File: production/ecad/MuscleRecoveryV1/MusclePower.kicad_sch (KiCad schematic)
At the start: 0 parts

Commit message: Added fuel guage schematic, may need adjustments
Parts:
- added C1: 1uF, symbol Device:C
- added CONN3G$1, CONN4G$1: Screw_Terminal_01x04, symbol Connector:Screw_Terminal_01x04
- added D1: GREEN, symbol Device:LED
- added IC1: LC709203FQH-01TWG, Package_DFN_QFN:WDFN-8-1EP_4x3mm_P0.65mm_EP2.4x1.8mm, symbol Battery_Management:LC709203FQH-01TWG
- added J1: Screw_Terminal_01x06, symbol Connector:Screw_Terminal_01x06
- added J2, J3: Screw_Terminal_01x02, symbol Connector:Screw_Terminal_01x02
- added R1, R3G$2, R3G$3: 10K, Resistor_SMD:R_0805_2012Metric, symbol Device:R
- added R3G$1, R3G$4: 10K, symbol Device:R
- added R4: 100, Resistor_SMD:R_0805_2012Metric, symbol Device:R
- added SJ1: SolderJumper_2_Open, symbol Jumper:SolderJumper_2_Open
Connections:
- new net: IC1.5 (T_{SW}), R4.1
- new net: R1.2, R4.2
- new net: IC1.6 (T_{SENSE}), R1.1
- new net: D1.1 (K), R3G$4.1
- new net: D1.2 (A), SJ1.1 (A)
- new net GND: C1.2, CONN3G$1.4 (Pin_4), CONN4G$1.4 (Pin_4), IC1.1 (TEST), IC1.2 (V_{SS}), J1.2 (Pin_2), J2.1 (Pin_1), J3.1 (Pin_1), R3G$4.2
- new net INT: IC1.4 (~{ALARMB}), J1.5 (Pin_5), R3G$3.2
- new net SCL: CONN3G$1.1 (Pin_1), CONN4G$1.1 (Pin_1), IC1.8 (SCL), J1.3 (Pin_3), R3G$1.2
- new net SDA: CONN3G$1.2 (Pin_2), CONN4G$1.2 (Pin_2), IC1.7 (SDA), J1.4 (Pin_4), R3G$2.2
- new net THERM: J1.6 (Pin_6)
- new net VCC: CONN3G$1.3 (Pin_3), CONN4G$1.3 (Pin_3), J1.1 (Pin_1), R3G$1.1, R3G$2.1, R3G$3.1, SJ1.2 (B)
- new net VDD: C1.1, J2.2 (Pin_2), J3.2 (Pin_2)

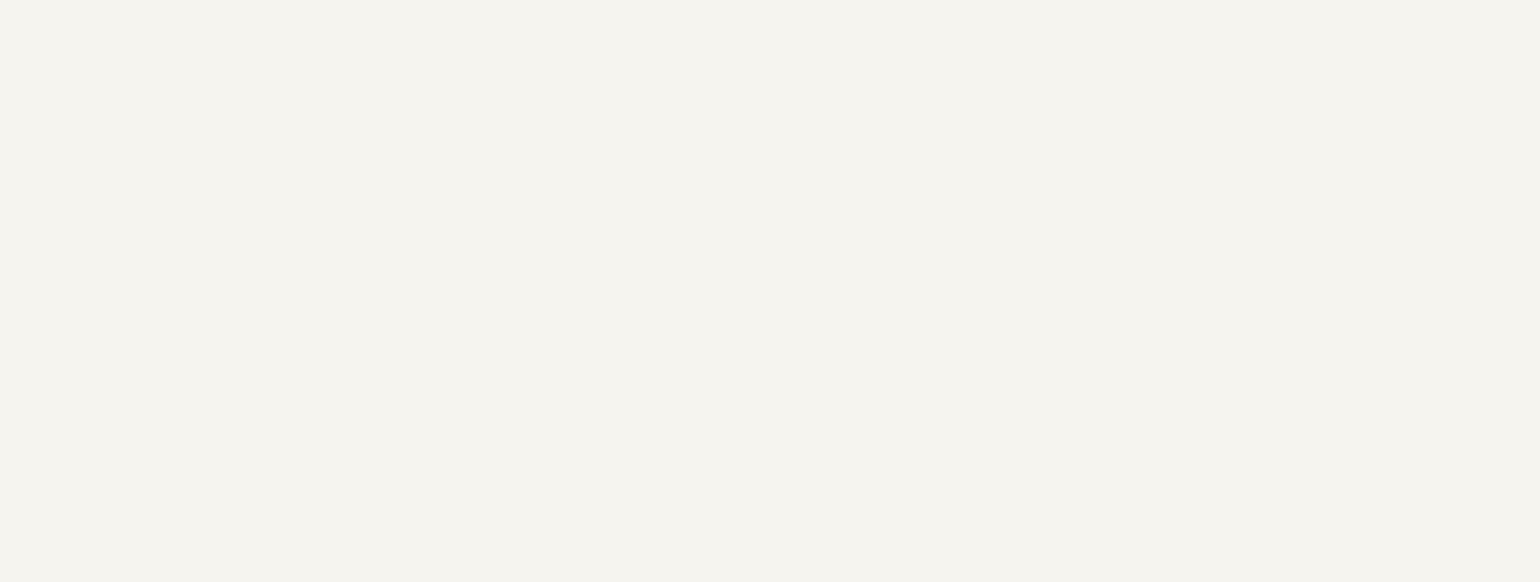
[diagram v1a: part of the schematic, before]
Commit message: Combined schematics together
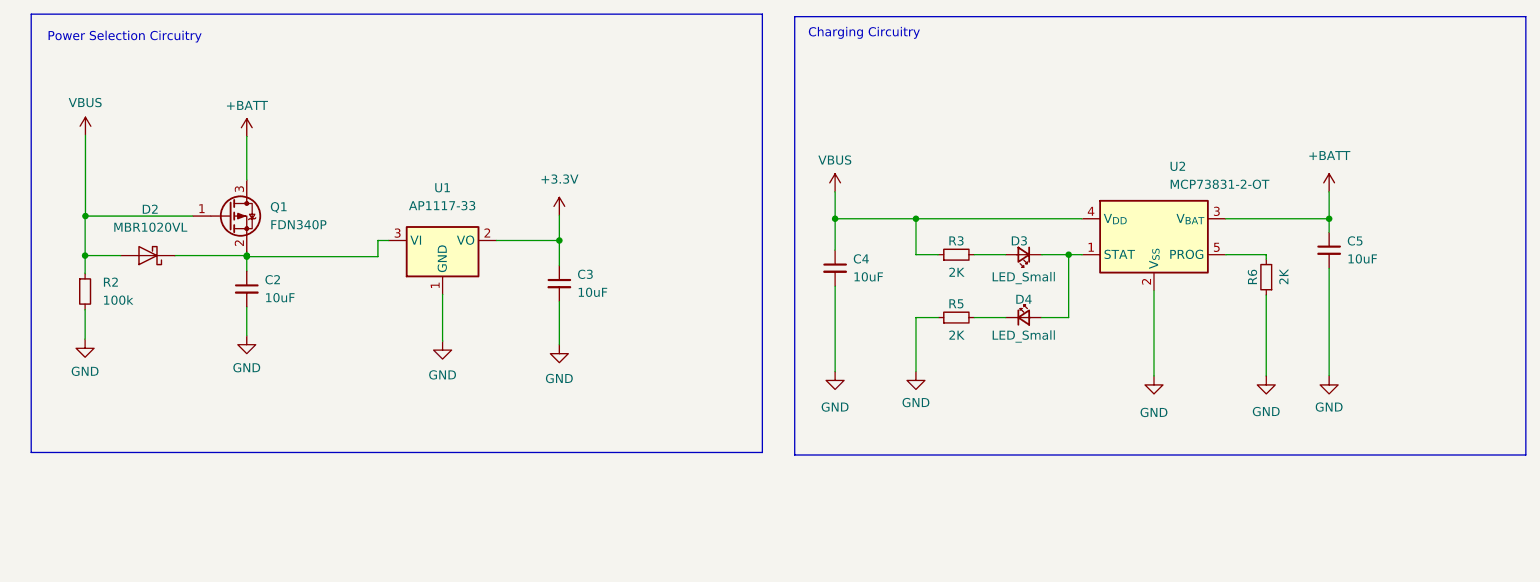
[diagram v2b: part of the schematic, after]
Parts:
- added C2, C3, C4, C5: 10uF, symbol Device:C_Small
- added D2: MBR1020VL, Diode_SMD:D_SOD-123F, symbol Diode:MBR1020VL
- added D3, D4: LED_Small, symbol Device:LED_Small
- added Q1: FDN340P, Package_TO_SOT_SMD:SOT-23, symbol Transistor_FET:FDN340P
- added R2: 100k, symbol Device:R_Small
- added R3, R5, R6: 2K, symbol Device:R_Small
- added U1: AP1117-33, Package_TO_SOT_SMD:SOT-223-3_TabPin2, symbol Regulator_Linear:AP1117-33
- added U2: MCP73831-2-OT, Package_TO_SOT_SMD:SOT-23-5, symbol Battery_Management:MCP73831-2-OT
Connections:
- net GND: now also C2.2, C3.2, C4.2, C5.2, R2.2, R5.1, R6.1, U1.1 (GND), U2.2 (V_{SS})
- new net: C2.1, D2.1 (K), Q1.2 (S), U1.3 (VI)
- new net: D4.1 (K), R5.2
- new net: D3.1 (K), D4.2 (A), U2.1 (STAT)
- new net: D3.2 (A), R3.2
- new net: R6.2, U2.5 (PROG)
- new net +3.3V: C3.1, U1.2 (VO)
- new net +BATT: C5.1, Q1.3 (D), U2.3 (V_{BAT})
- new net VBUS: C4.1, D2.2 (A), Q1.1 (G), R2.1, R3.1, U2.4 (V_{DD})
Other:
- note added: "Charging Circuitry"
- note added: "Power Selection Circuitry"

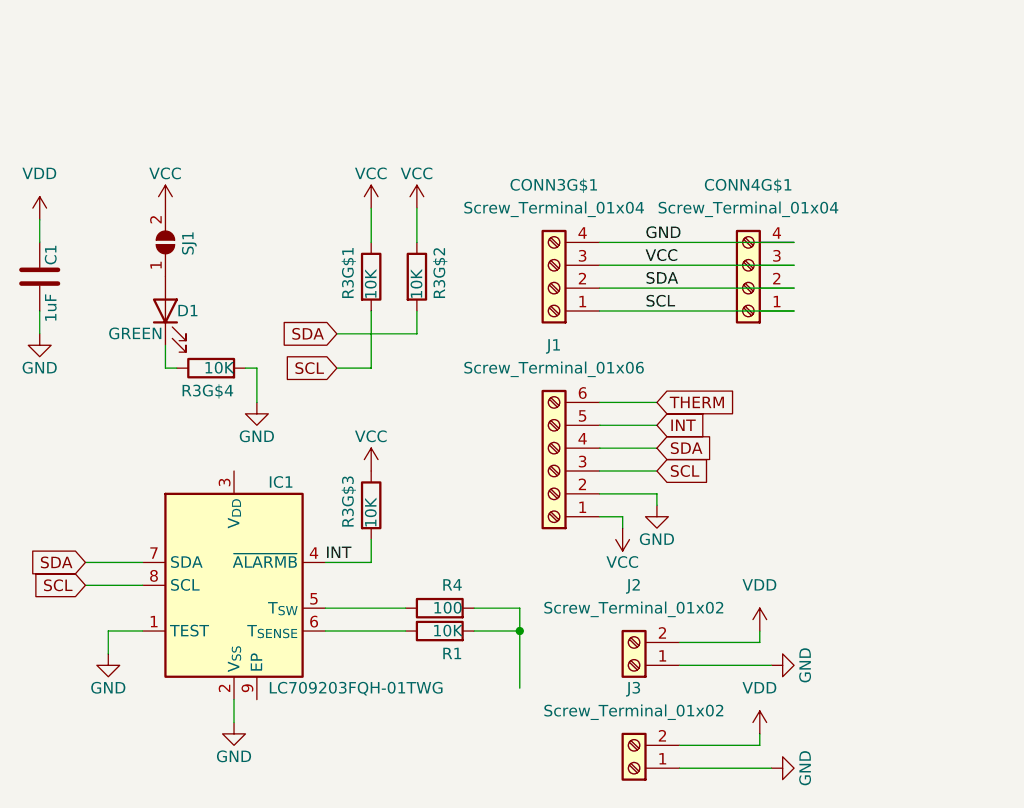
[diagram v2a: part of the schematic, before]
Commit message: changes to fuel guage schematic and quick draft of ecg schematic - not finished
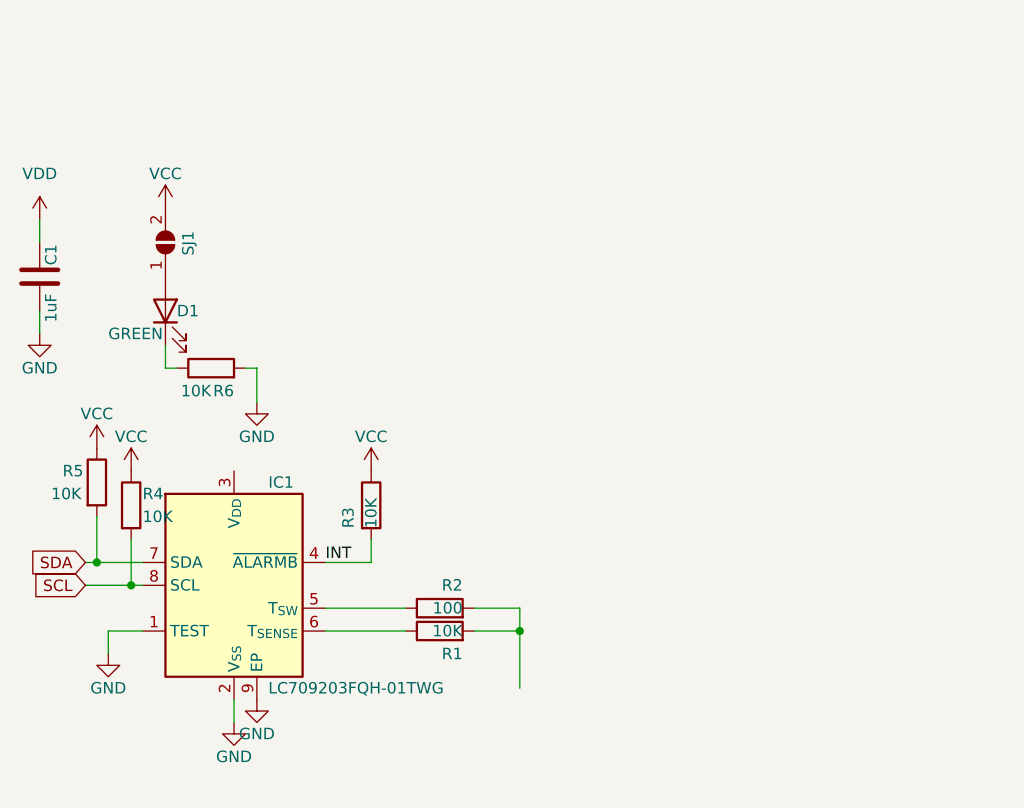
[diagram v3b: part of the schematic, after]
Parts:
- removed CONN3G$1, CONN4G$1: Screw_Terminal_01x04, symbol Connector:Screw_Terminal_01x04
- removed J1: Screw_Terminal_01x06, symbol Connector:Screw_Terminal_01x06
- removed J2, J3: Screw_Terminal_01x02, symbol Connector:Screw_Terminal_01x02
- removed R3G$1: 10K, symbol Device:R
- removed R3G$2: 10K, Resistor_SMD:R_0805_2012Metric, symbol Device:R
- added R4, R5: 10K, symbol Device:R
- renumbered R4 to R2, R3G$3 to R3, R3G$4 to R6
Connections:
- net GND: now also IC1.9 (EP)
- net SCL: now also R4.2
- net SDA: now also R5.2
- net VCC: now also R4.1, R5.1

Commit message: Testing Commit for Andy
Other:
- note added: "Hello This is test to see if andy can properly committ"
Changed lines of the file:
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@@
     (fill (type none))
+  )
+  (text "Hello This is test to see if andy can properly committ"
+    (at 50.8 112.395 0)
+    (effects (font (size 3.81 3.81)) (justify left bottom))
   )
   (text "Charging Circuitry\n" (at 126.365 20.701 0)

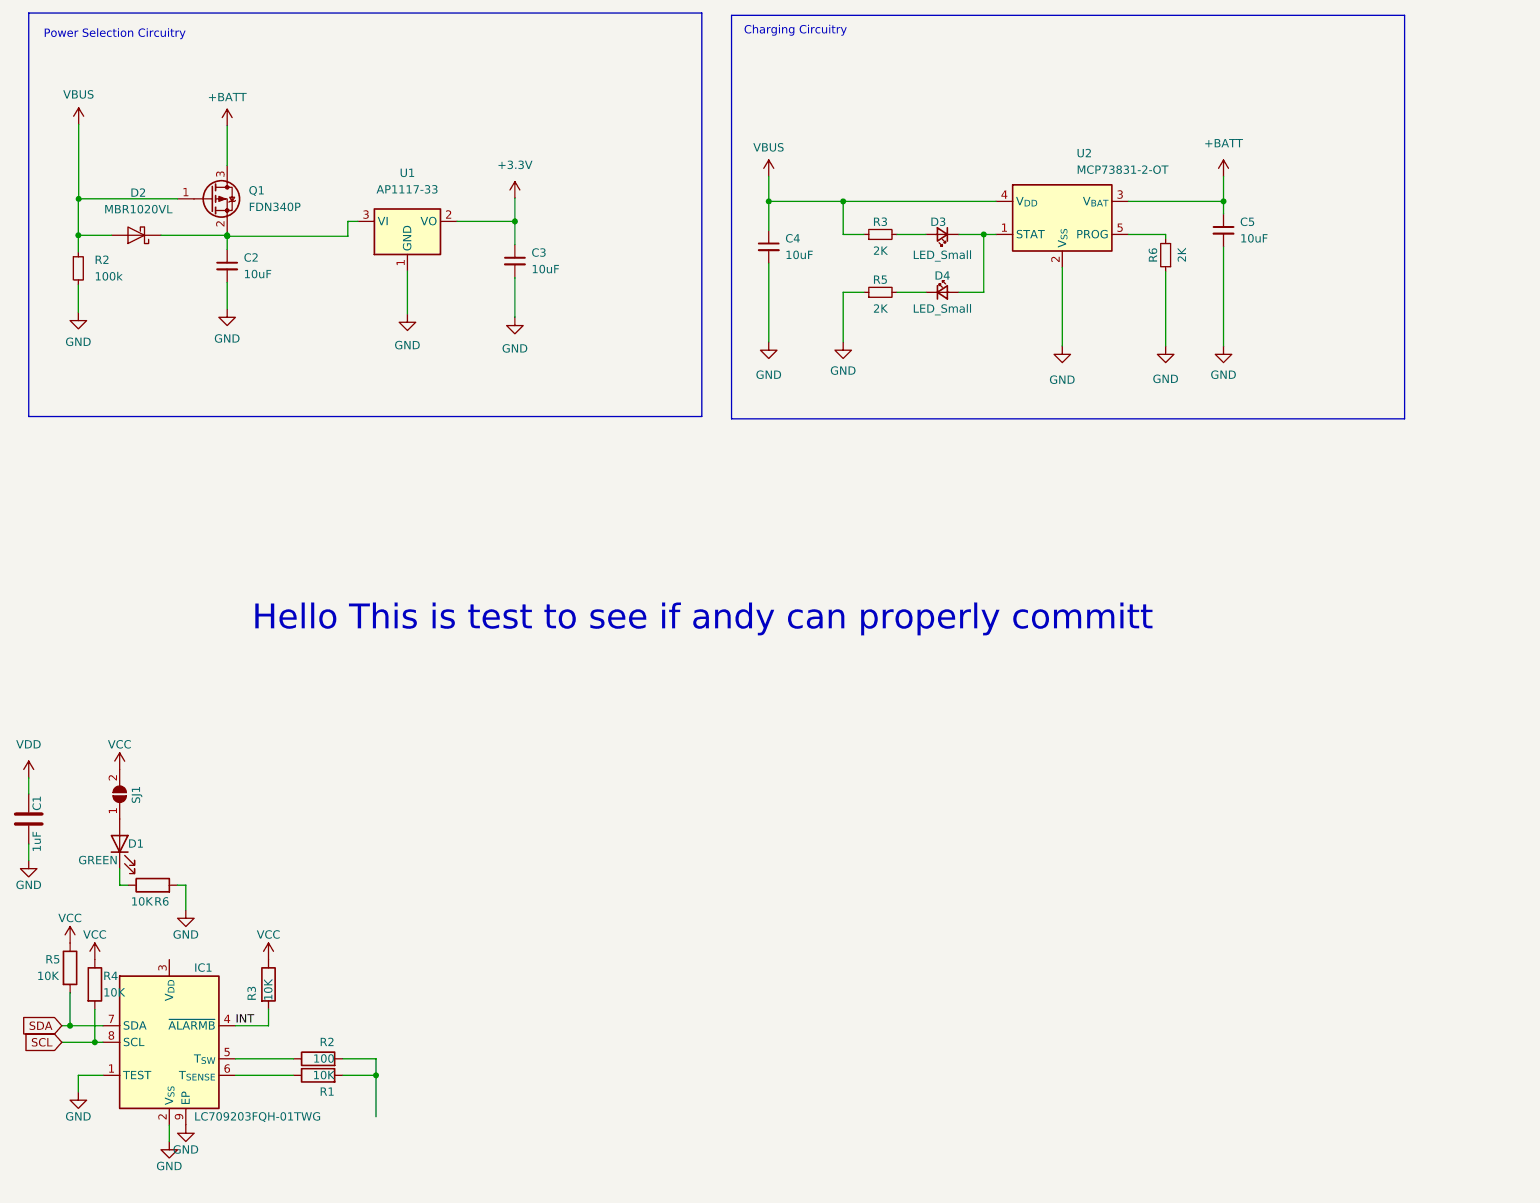
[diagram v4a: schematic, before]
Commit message: Pushing ESP-32 Implementation placed on the power page
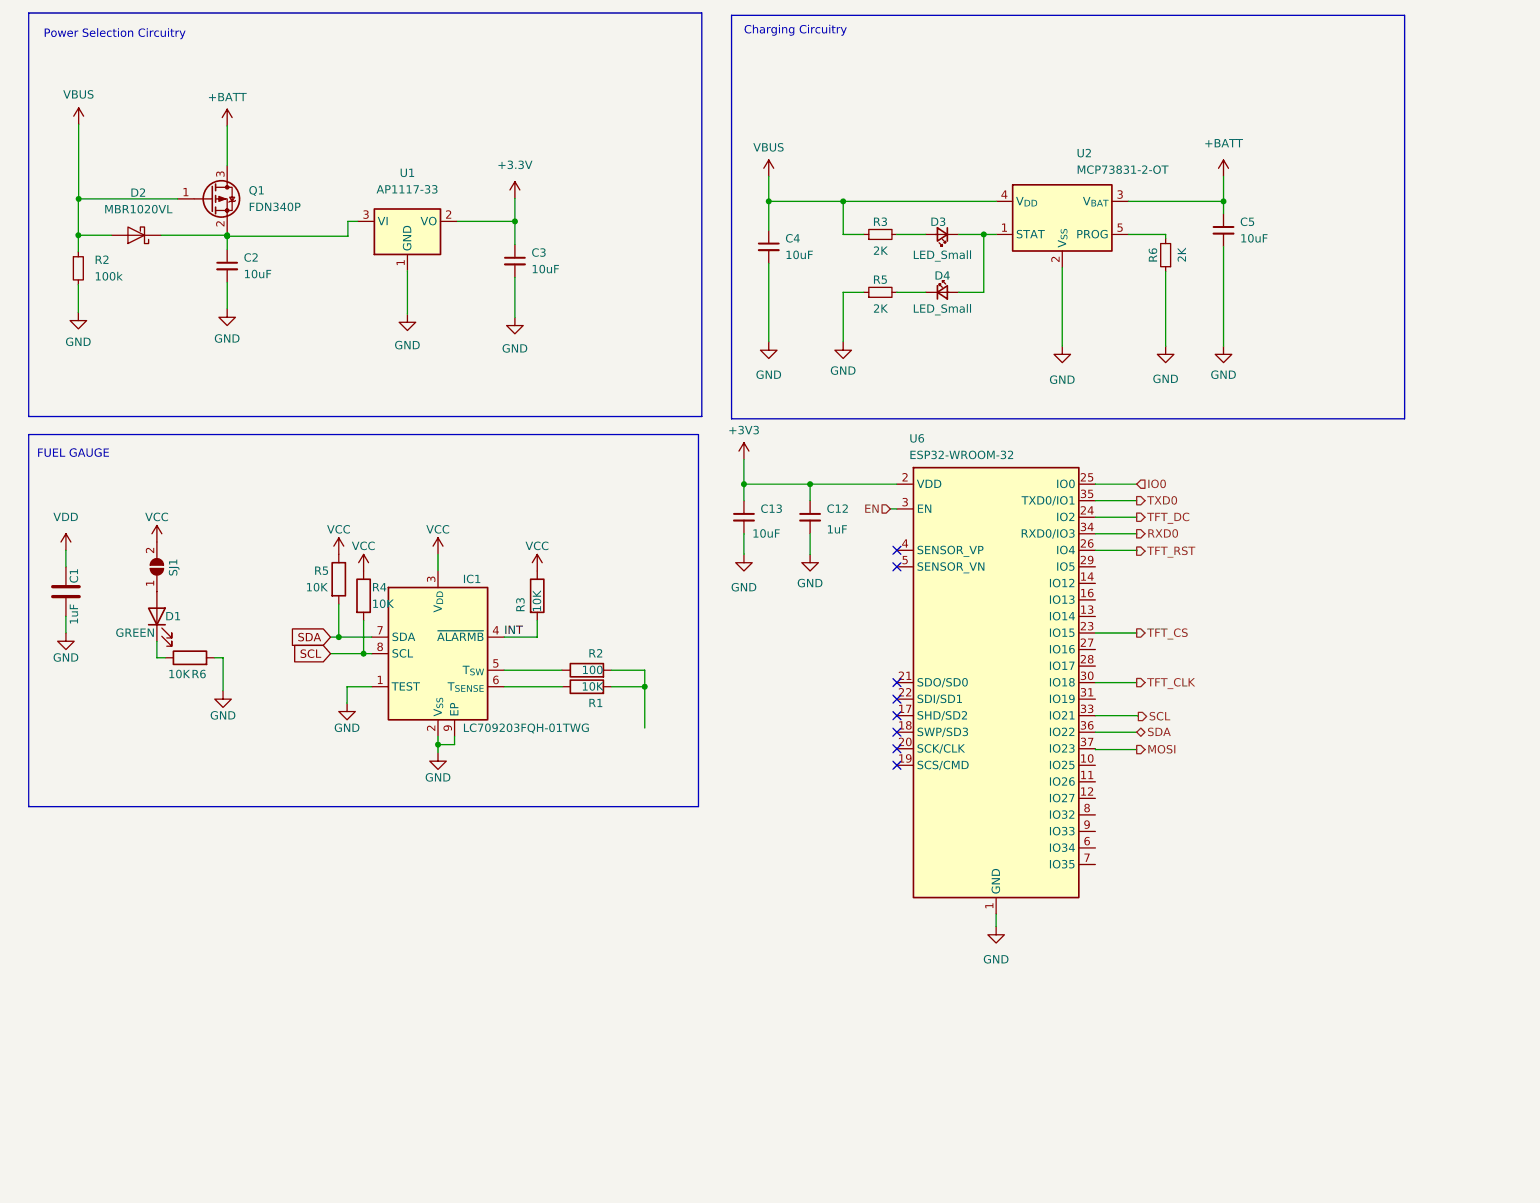
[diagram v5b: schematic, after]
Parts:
- added C12: 1uF, symbol Device:C_Small
- added C13: 10uF, symbol Device:C_Small
- added U6: ESP32-WROOM-32, RF_Module:ESP32-WROOM-32, symbol RF_Module:ESP32-WROOM-32
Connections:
- net GND: now also C12.2, C13.2, U6.1 (GND), U6.15 (GND), U6.38 (GND), U6.39 (GND)
- net SCL: now also U6.33 (IO21)
- net SDA: now also U6.36 (IO22)
- net VCC: now also IC1.3 (V_{DD})
- new net +3V3: C12.1, C13.1, U6.2 (VDD)
- new net EN: U6.3 (EN)
- new net IO0: U6.25 (IO0)
- new net MOSI: U6.37 (IO23)
- new net RXD0: U6.34 (RXD0/IO3)
- new net TFT_CLK: U6.30 (IO18)
- new net TFT_CS: U6.23 (IO15)
- new net TFT_DC: U6.24 (IO2)
- new net TFT_RST: U6.26 (IO4)
- new net TXD0: U6.35 (TXD0/IO1)
- no-connect marks 0 -> 8
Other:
- note added: "FUEL GAUGE"
- note removed: "Hello This is test to see if andy can properly committ"
- moved on the sheet: C1, D1, IC1, R1, R2, R3, R4, R5, R6, SJ1

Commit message: Revert "Display commit 1"
This reverts commit 52e50f7827ccbfa861bea7a8a003d131d02fed89.
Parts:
- removed C1: 1uF, symbol Device:C
- removed C12: 1uF, symbol Device:C_Small
- removed C13, C2, C3, C4: 10uF, symbol Device:C_Small
- removed R1, R3: 10K, Resistor_SMD:R_0805_2012Metric, symbol Device:R
- removed R2: 100, Resistor_SMD:R_0805_2012Metric, symbol Device:R
- removed R2: 100k, symbol Device:R_Small
- removed R3, R5, R6: 2K, symbol Device:R_Small
- removed R4, R5, R6: 10K, symbol Device:R
- removed U6: ESP32-WROOM-32, RF_Module:ESP32-WROOM-32, symbol RF_Module:ESP32-WROOM-32
- added BATT1: TestPoint, symbol Connector:TestPoint
- added C15, C16, C18: 10uF, symbol Device:C_Small
- added C17: 1uF, symbol Device:C
- added R32: 100k, symbol Device:R_Small
- added R33, R38, R39: 2K, symbol Device:R_Small
- added R34, R35, R37: 10K, symbol Device:R
- added R36: 10K, Resistor_SMD:R_0805_2012Metric, symbol Device:R
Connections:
- net VCC is gone; now on net +BATT: IC1.3 (V_{DD}), SJ1.2 (B)
- net +3.3V: now also C16.1
- net +BATT: now also BATT1.1, C17.1, R34.1, R35.1, R36.1
- net GND: now also C15.2, C16.2, C17.2, C18.2, R32.2, R33.1, R37.2, R39.1
- net INT: now also R36.2
- net SCL: now also R35.2
- net SDA: now also R34.2
- net VBUS: now also C18.1, R32.1, R38.1
- net at D2.1 (K), Q1.2 (S), U1.3 (VI): now also C15.1
- net at D1.1 (K): now also R37.1
- net at D4.1 (K): now also R39.2
- net at D3.2 (A): now also R38.2
- net at U2.5 (PROG): now also R33.2
- no-connect marks 8 -> 2
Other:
- moved on the sheet: D1, D2, D3, D4, IC1, Q1, SJ1, U1, U2
